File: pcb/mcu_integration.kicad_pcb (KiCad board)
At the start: 4 copper layers, 100 x 100 mm, 98 parts, among them IC1 TL7660IDGKR, IC10 AD844_OPAMP_MEL, IC2 TL081IDT, IC3 FOD814_OPTO_NOSHD, IC4 UA78M33CDCYG3, IC5 FOD814_OPTO_MEL, IC6 AD844_OPAMP_AL, IC7 FOD814_OPTO_AL, IC8 AD844_OPAMP_NOSHD, J1 Micro_SD_Card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

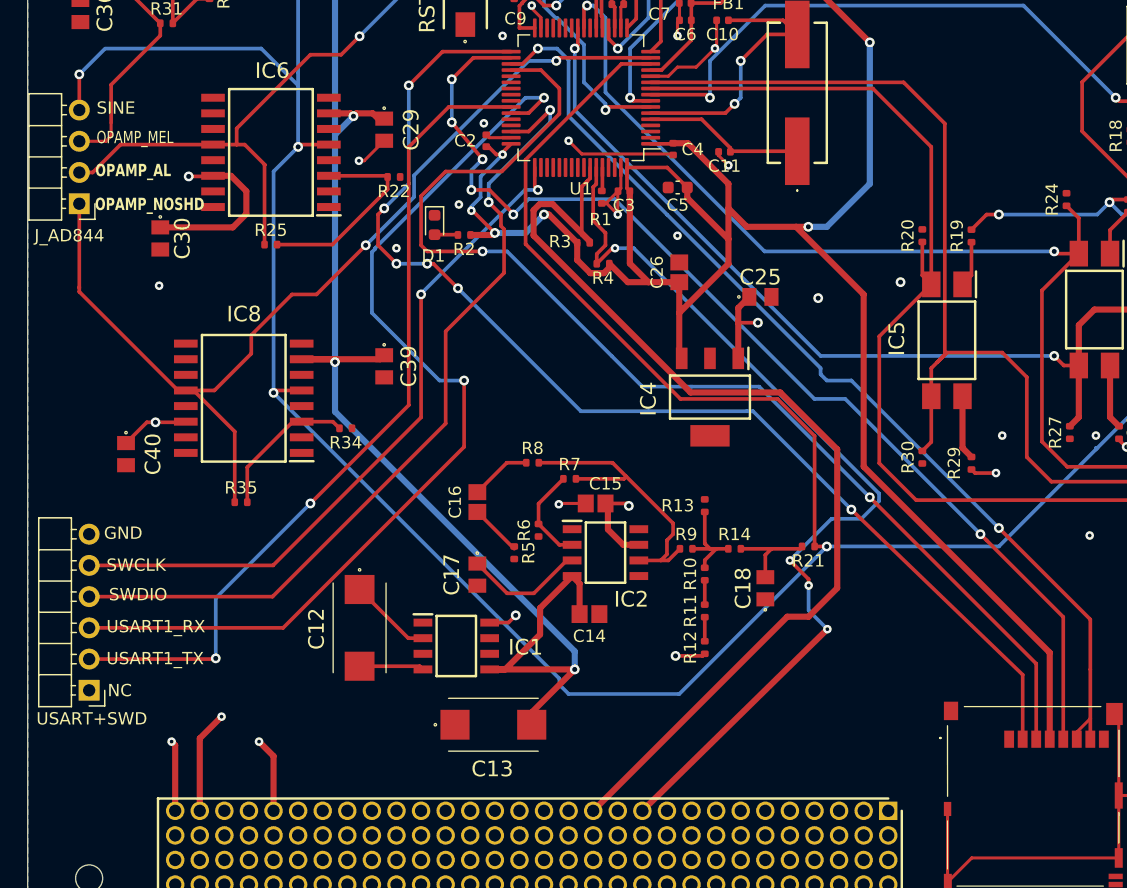
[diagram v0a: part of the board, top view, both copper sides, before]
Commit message: Implemented mosfet, decoupling
Please review functionality
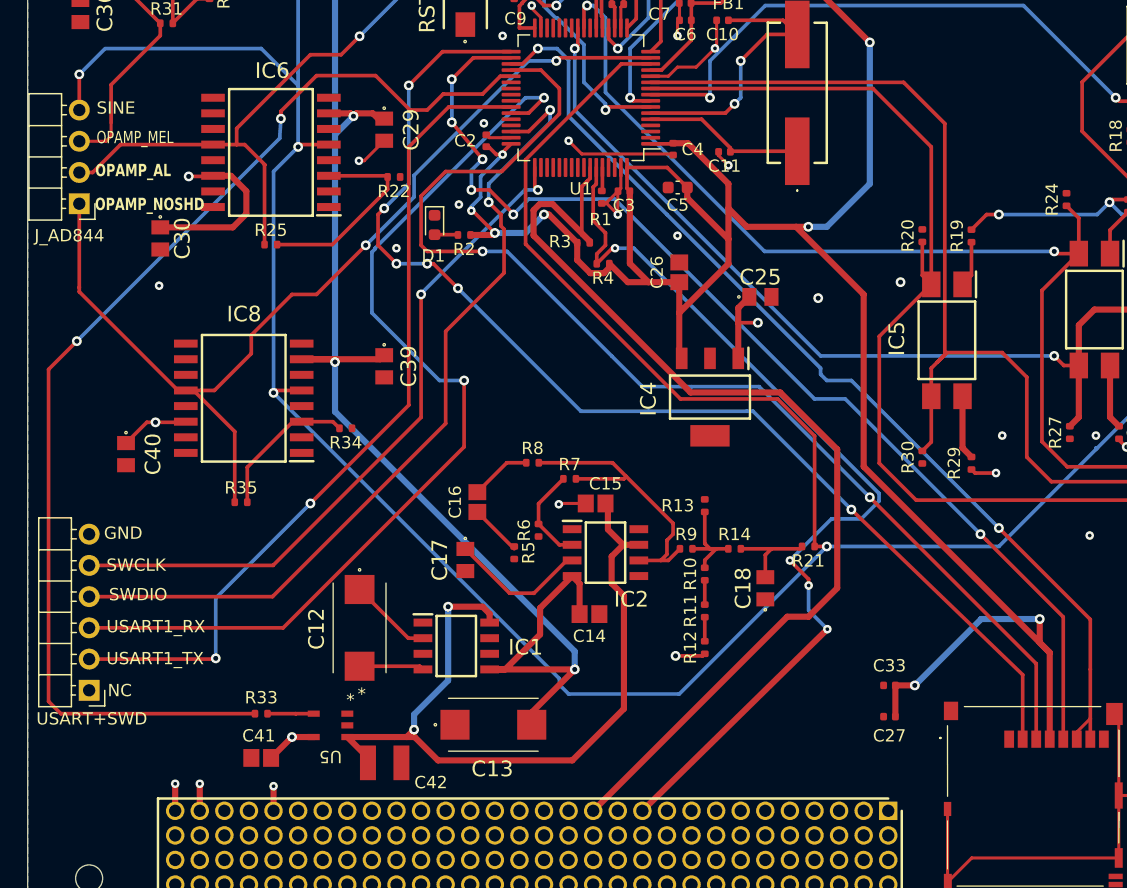
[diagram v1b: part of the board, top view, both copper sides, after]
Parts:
- added C27: 100n, Capacitor_SMD:C_0402_1005Metric, F.Cu at (135.1, 116.8)
- added C33: 1u, Capacitor_SMD:C_0402_1005Metric, F.Cu at (135.1, 114.3)
- added C41: 0.1u, capstone:CAPC220145_88N_KEM-0.1u, F.Cu at (84.0, 120.2)
- added C42: 150u, capstone:CAPC3225X280N_150U, F.Cu at (94.0, 120.6)
- added R33: 200, Resistor_SMD:R_0402_1005Metric, F.Cu at (84.0, 116.6)
- added U5: TPS2069CDBVR_MOSFET, capstone:DBV5_TEX_MF, F.Cu at (89.6, 117.5)
- R22, R28, R34: value 1k -> 100k
- R25, R31, R35: value 100k -> 1k
- moved C17 1.54 mm to (100.6, 104.1)
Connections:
- C15 pad 1: +5V -> MOSFET_OUTPUT
- IC1 pad 8: +5V -> MOSFET_OUTPUT
- IC2 pad 7: +5V -> MOSFET_OUTPUT
- U1 pad 37: unconnected-(U1-PC6-Pad37) -> MOSFET_CONTROL
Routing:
- net MOSFET_CONTROL: track 0.00 -> 95.3 mm, vias 0 -> 2
- net MOSFET_OUTPUT: track 0.00 -> 63.5 mm, vias 0 -> 2
- net 3.3V Output: track 199.1 -> 218.7 mm, vias 8 -> 10
- net GND: track 99.2 -> 89.4 mm
- net +5V: track 106.7 -> 97.1 mm, vias 14 -> 13
- net Net-(U5-EN/*EN): track 0.00 -> 3.89 mm
- net Net-(IC2-NON-INVERTING_INPUT): track 9.82 -> 11.3 mm

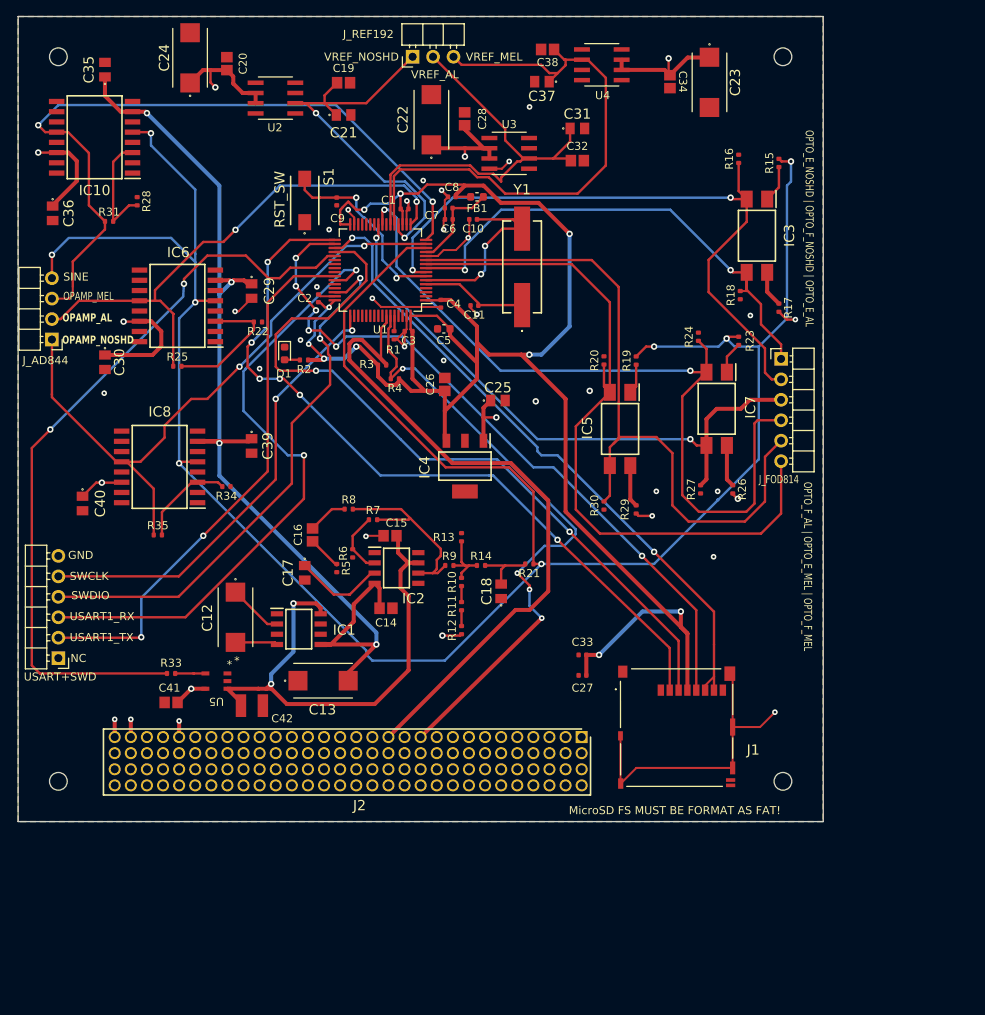
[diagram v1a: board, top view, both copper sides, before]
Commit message: wire placement, inital revisions
made it more PCB ready with spacing and such
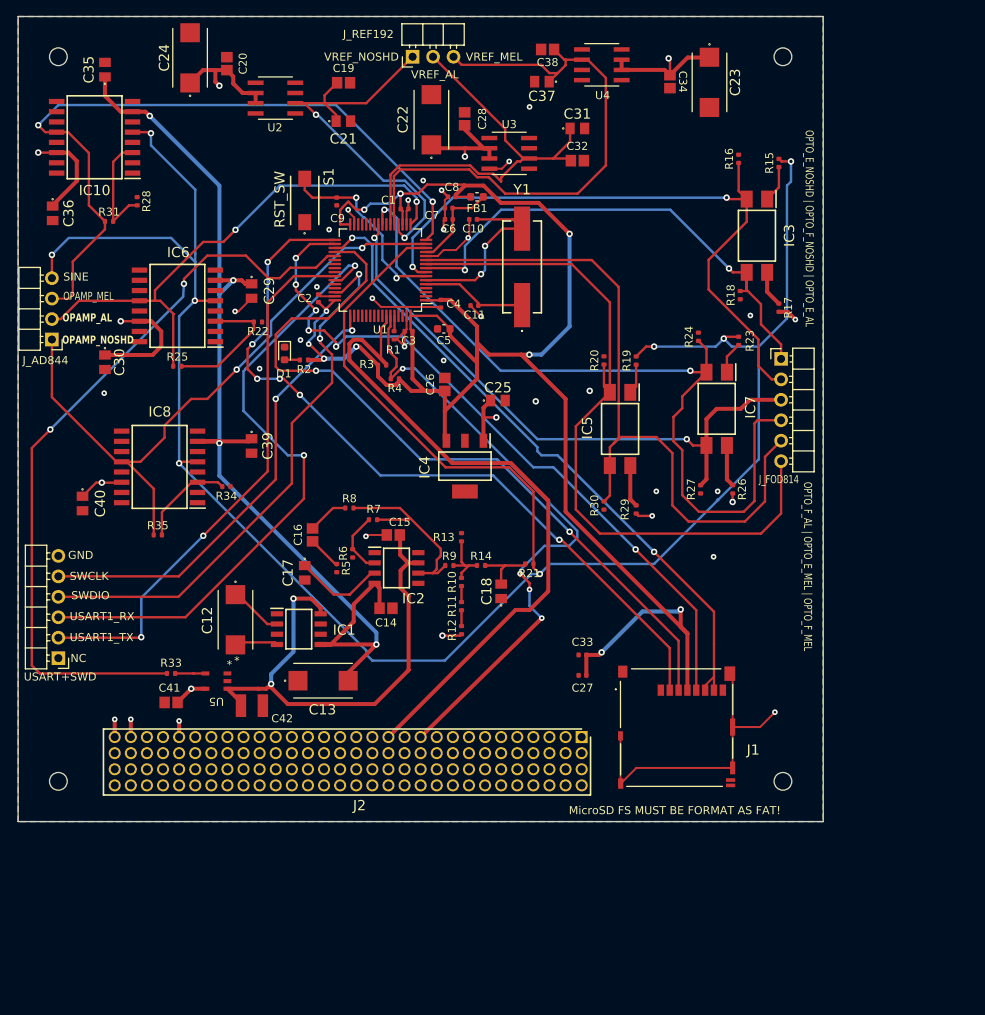
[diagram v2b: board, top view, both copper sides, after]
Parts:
- moved C21 0.77 mm to (105.4, 48.0)
- moved C15 0.42 mm to (111.6, 99.4)
- moved C12 0.31 mm to (92.0, 109.9)
- moved R8 0.16 mm to (106.2, 96.0)
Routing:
- net GND: track 89.4 -> 90.4 mm
- net ADC1_IN0_SINE: track 285.6 -> 286.5 mm
- net /SWDIO: track 68.8 -> 69.6 mm
- net ADC1_IN14_OPTO_F_AL: track 98.3 -> 99.1 mm

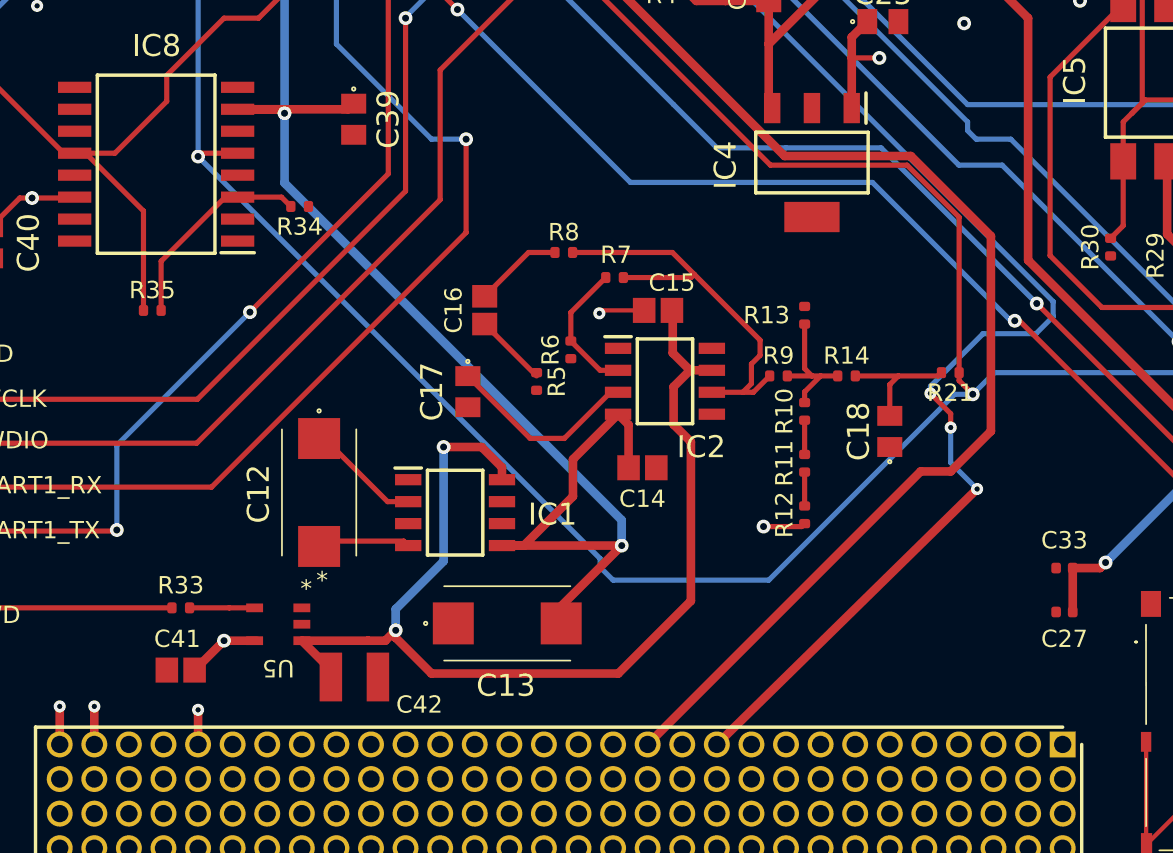
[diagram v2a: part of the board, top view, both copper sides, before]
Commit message: MOSFET connections updated (#13)
* MOSFET connections updated

updated the MOSFET connection to control the 5V plane and added a separate line going directly to the 3.3V regulator.

* rotate U5 silk

---------

Co-authored-by: Karim Ait-Allaoua <kaitallaoua@gmail.com>
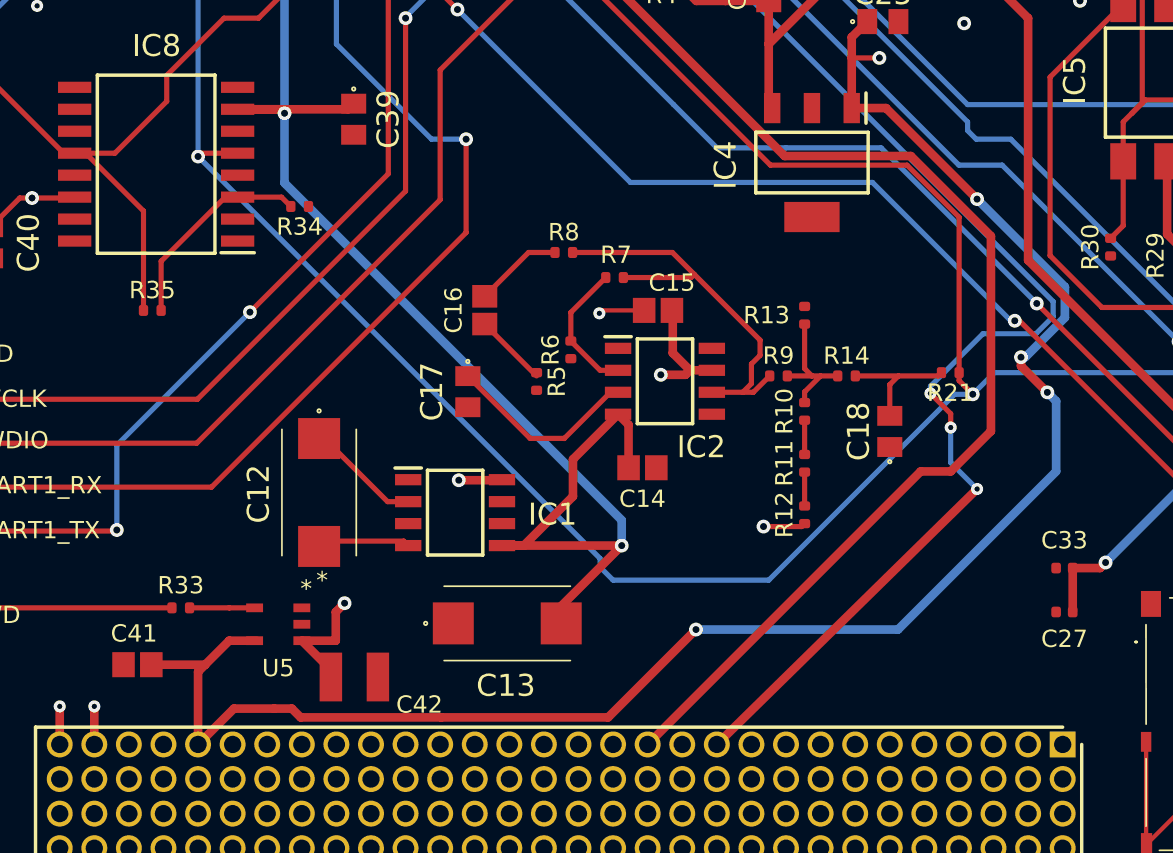
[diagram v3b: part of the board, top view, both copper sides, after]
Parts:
- moved C41 2.52 mm to (81.5, 119.9)
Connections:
- C15 pad 1: MOSFET_OUTPUT -> +5V
- C42 pad 1: MOSFET_OUTPUT -> +5V
- IC1 pad 8: MOSFET_OUTPUT -> +5V
- IC2 pad 7: MOSFET_OUTPUT -> +5V
- U5 pad 1: MOSFET_OUTPUT -> +5V
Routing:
- net +5V: track 97.3 -> 204.9 mm, vias 13 -> 18
- net MOSFET_OUTPUT: track 63.9 -> 0.00 mm, vias 2 -> 0

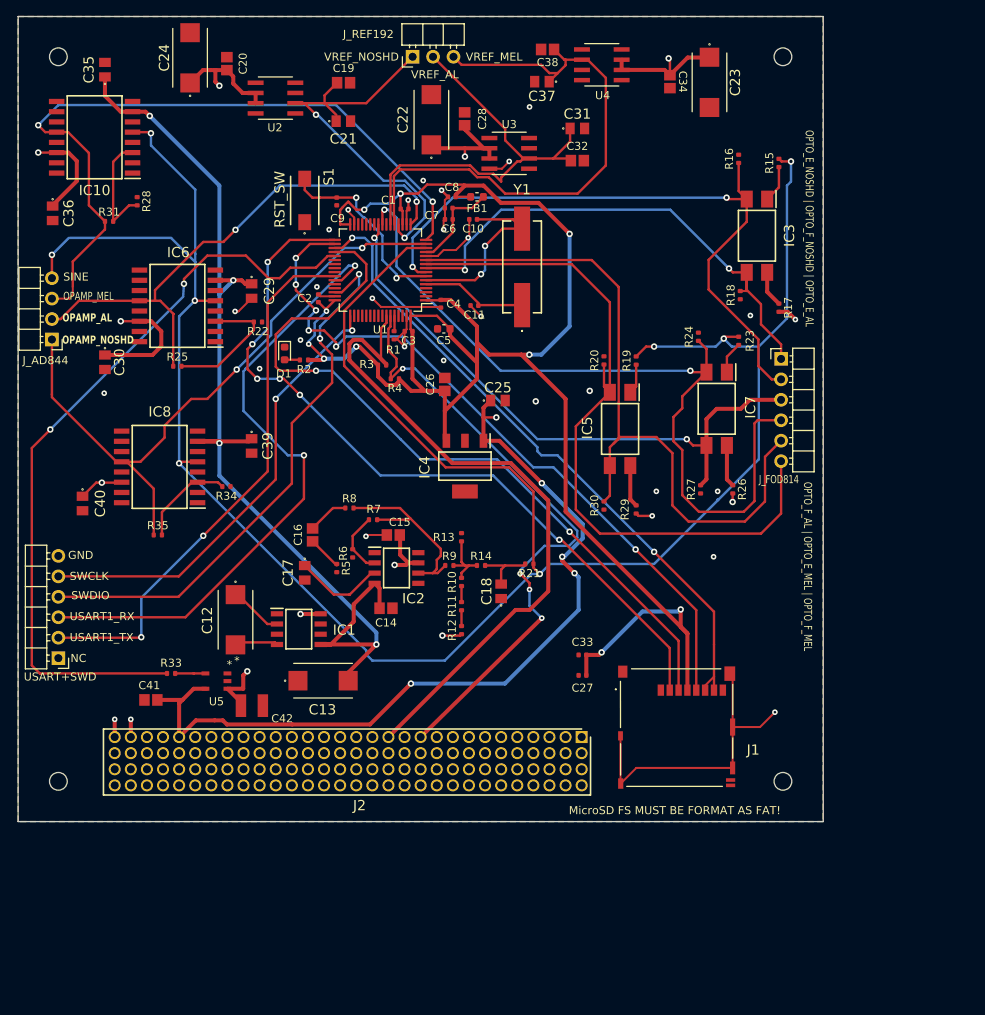
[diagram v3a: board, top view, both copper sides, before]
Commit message: Updated vias from micro to through hole
Please check to ensure there are no more micro vias.
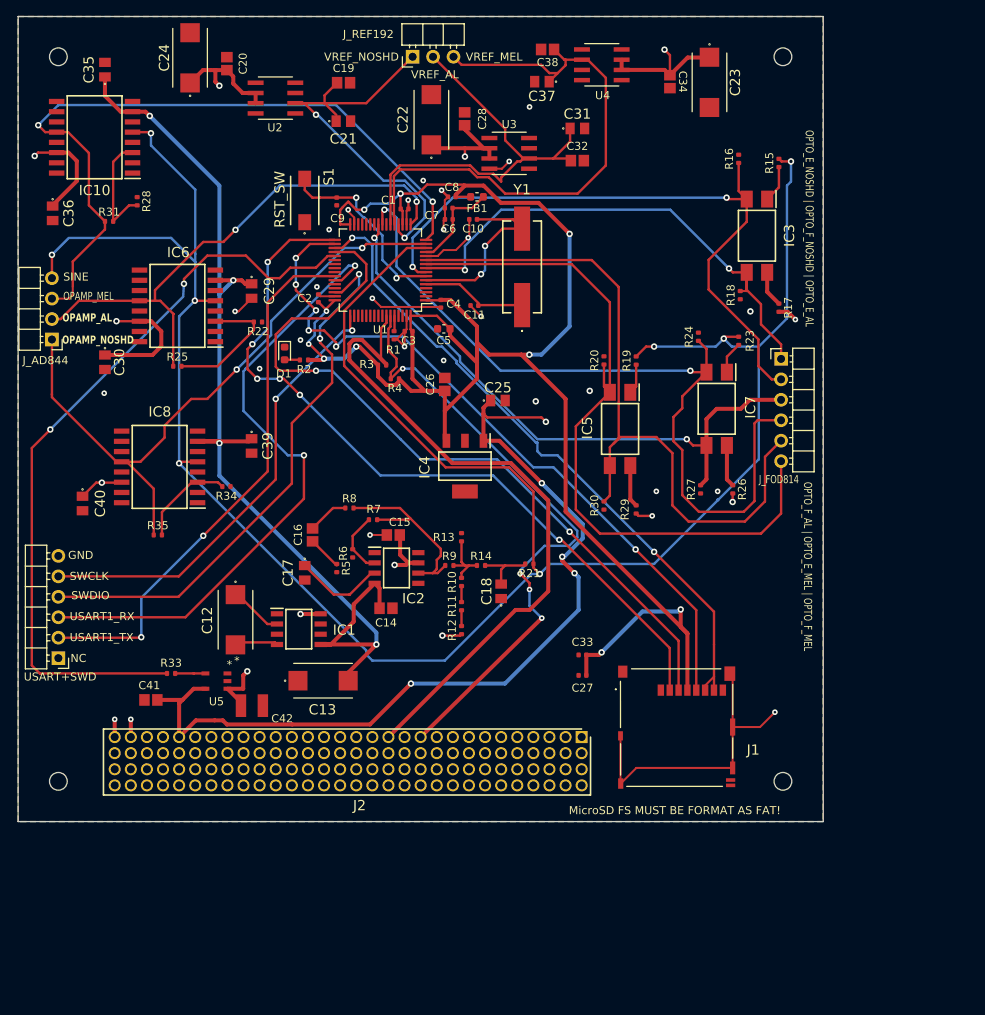
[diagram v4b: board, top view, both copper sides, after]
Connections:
- IC3 pad 3: ADC1_IN11_OPTO_E_NOSHD -> GND
- J_FOD814 pad 1: ADC1_IN11_OPTO_E_NOSHD -> GND
- R18 pad 2: ADC1_IN11_OPTO_E_NOSHD -> GND
- U1 pad 9: ADC1_IN11_OPTO_E_NOSHD -> GND
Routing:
- net GND: track 90.4 -> 189.4 mm, vias 28 -> 29
- net ADC1_IN11_OPTO_E_NOSHD: track 63.7 -> 0.00 mm, vias 2 -> 0
- net +5V: track 204.9 -> 240.4 mm

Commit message: done layout/ratsnet
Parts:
- J3, J_FOD814: footprint Connector_PinHeader_2.54mm:PinHeader_1x06_P2.54mm_Horizontal -> Connector_PinHeader_2.54mm:PinHeader_1x06_P2.54mm_Vertical
- J_AD844: footprint Connector_PinHeader_2.54mm:PinHeader_1x04_P2.54mm_Horizontal -> Connector_PinHeader_2.54mm:PinHeader_1x04_P2.54mm_Vertical
- J_REF192: footprint Connector_PinHeader_2.54mm:PinHeader_1x03_P2.54mm_Horizontal -> Connector_PinHeader_2.54mm:PinHeader_1x03_P2.54mm_Vertical
- moved C24 102.3 mm to (126.4, 134.3), turned to -90 degrees
- moved C20 93.7 mm to (126.8, 127.4), turned to 0 degrees
- moved C41 92.1 mm to (164.0, 78.9)
- moved C23 91.7 mm to (141.2, 134.4)
- moved R33 90.0 mm to (168.0, 84.3), turned to 0 degrees
- moved C22 88.3 mm to (133.8, 134.4), turned to -90 degrees
- moved C34 84.7 mm to (140.8, 127.6), turned to 0 degrees
- moved C35 82.3 mm to (89.0, 122.8), turned to -90 degrees
- moved U5 81.6 mm to (163.8, 83.5), turned to 0 degrees
- moved U2 81.4 mm to (126.6, 121.0), turned to 90 degrees
- moved J3 81.4 mm to (148.5, 93.1)
- moved C28 81.0 mm to (133.8, 127.6), turned to 0 degrees
- moved U4 79.9 mm to (141.1, 120.9), turned to 90 degrees
- moved C29 76.9 mm to (102.1, 145.6), turned to 90 degrees
- moved R25 76.8 mm to (118.0, 147.7)
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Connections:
- C42 pad 1: +5V -> MOSFET_OUTPUT
- IC1 pad 8: +5V -> MOSFET_OUTPUT
- IC3 pad 3: GND -> ADC1_IN11_OPTO_E_NOSHD
- J1 pad 6: /SPI2_MISO -> GND
- J_FOD814 pad 1: GND -> ADC1_IN11_OPTO_E_NOSHD
- R18 pad 2: GND -> ADC1_IN11_OPTO_E_NOSHD
- U1 pad 9: GND -> ADC1_IN11_OPTO_E_NOSHD
- U5 pad 1: +5V -> MOSFET_OUTPUT
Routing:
- net ADC1_IN0_SINE: track 286.5 -> 0.00 mm, vias 8 -> 0
- net +5V: track 240.4 -> 0.00 mm, vias 18 -> 0
- net 3.3V Output: track 218.9 -> 0.00 mm, vias 10 -> 0
- net GND: track 189.4 -> 0.00 mm, vias 29 -> 0
- net -5V Output: track 129.9 -> 0.00 mm, vias 4 -> 0
- net ADC1_IN14_OPTO_F_AL: track 99.1 -> 0.00 mm, vias 2 -> 0
- net /SPI2_CS_NSS: track 95.8 -> 0.00 mm, vias 6 -> 0
- net MOSFET_CONTROL: track 95.3 -> 0.00 mm, vias 2 -> 0
- net /SPI2_MOSI: track 94.9 -> 0.00 mm, vias 2 -> 0
- net ADC1_IN2_OPAMP_MEL: track 90.7 -> 0.00 mm, vias 2 -> 0
- net ADC1_IN12_OPTO_F_MEL: track 90.3 -> 0.00 mm
- net /SPI2_SCK: track 89.8 -> 0.00 mm, vias 6 -> 0
- net ADC1_IN13_OPTO_E_MEL: track 89.4 -> 0.00 mm
- net OBC_I2C_SCL: track 85.4 -> 0.00 mm
- net ADC1_IN10_OPTO_F_NOSHD: track 82.9 -> 0.00 mm, vias 2 -> 0
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- removed copper zone on In2.Cu, net +5V
- removed copper zone on B.Cu, net GND
- removed copper zone on F.Cu, net GND
- removed copper zone on In1.Cu, net GND
- removed copper zone on In2.Cu, net GND
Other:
- board outline removed
